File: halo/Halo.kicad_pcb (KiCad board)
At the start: 2 copper layers, 85 x 93 mm, 83 parts, among them J1 USB-C 16P, J2 5V / GND alt, Q1 ALS-PT19-315C, SW1 RESET, SW2 BOOT, SW3 USER, U1 ESP32-C3-MINI-1-N4, U2 AMS1117-3.3, U3 74AHCT1G125

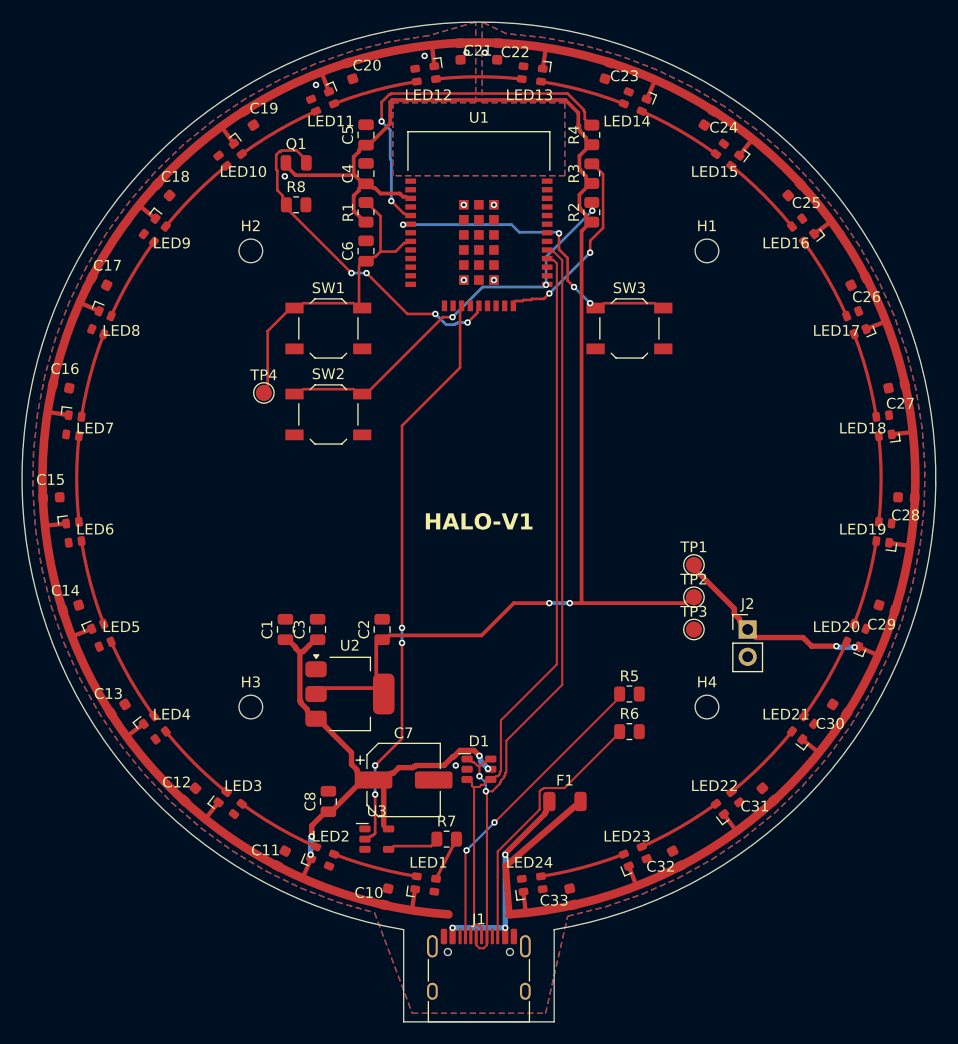
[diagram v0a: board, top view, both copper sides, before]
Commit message: Halo : empreintes ESP32-C3-MINI-1 et WS2812B-2020 d'apres les datasheets, anneau reroute, Gerbers
Verification des empreintes maison contre les datasheets avant les Gerbers :

- ESP32-C3-MINI-1 : l'empreinte "de memoire" placait les 53 broches sur le bord
  du module ; le vrai land pattern (datasheet Espressif v2.2 fig. 11-1, identique
  a espressif/kicad-libraries) a les broches en retrait a x = +/-5.9, rangees
  y = -2.2 / 7.6, masse centrale 3 x 3 (pad 49, un via par pastille), 4 pastilles
  d'angle raccordees par un court segment. Zone antenne 5.4 mm : encoche sans
  cuivre allongee a y = -26.9, keepout de routage ajuste. Table des broches
  (3-1) confirmee identique au schema.
- WS2812B-2020 Worldsemi (LCSC C965555) : brochage reel 1 DO, 2 GND, 3 DI,
  4 VDD, DI et VDD du meme cote. Symbole et empreinte (0.7 x 0.7) refaits ;
  l'anneau tourne desormais dans le sens trigonometrique depuis LED1 en bas a
  droite (impose par le brochage), data DO -> DI en segments droits, 100nF a
  r = 40. Le firmware ne presume rien de la position de LED1.
- SOT-23-5/6 et fusible 1206 aux cotes des bibliotheques KiCad 10 ; trous de
  fixation renommes MountingHole_2.2mm_M2.
- Placement : decouplage et pull-ups le long des vraies broches, F1/C7 et
  U3/R7/C8 permutes gauche/droite pour LED1 a droite. Boutons inchanges (coque).
- Librairies du projet : Halo.kicad_sym, Halo.pretty, sym-lib-table et
  fp-lib-table generes par gen_kicad_libs.py ; ERC a 0.
- Routage du centre refait par route_center.py ; drc.py 0 erreur ; kicad-cli
  pcb drc --refill-zones : 0 non connecte, 0 erreur.
- Gerbers, percage Excellon et fichier de position (kicad-cli 10.0.3) dans
  halo/GERBER_HALO et halo/Halo_GERBER.zip.

Co-Authored-By: Claude Fable 5.1 <noreply@anthropic.com>
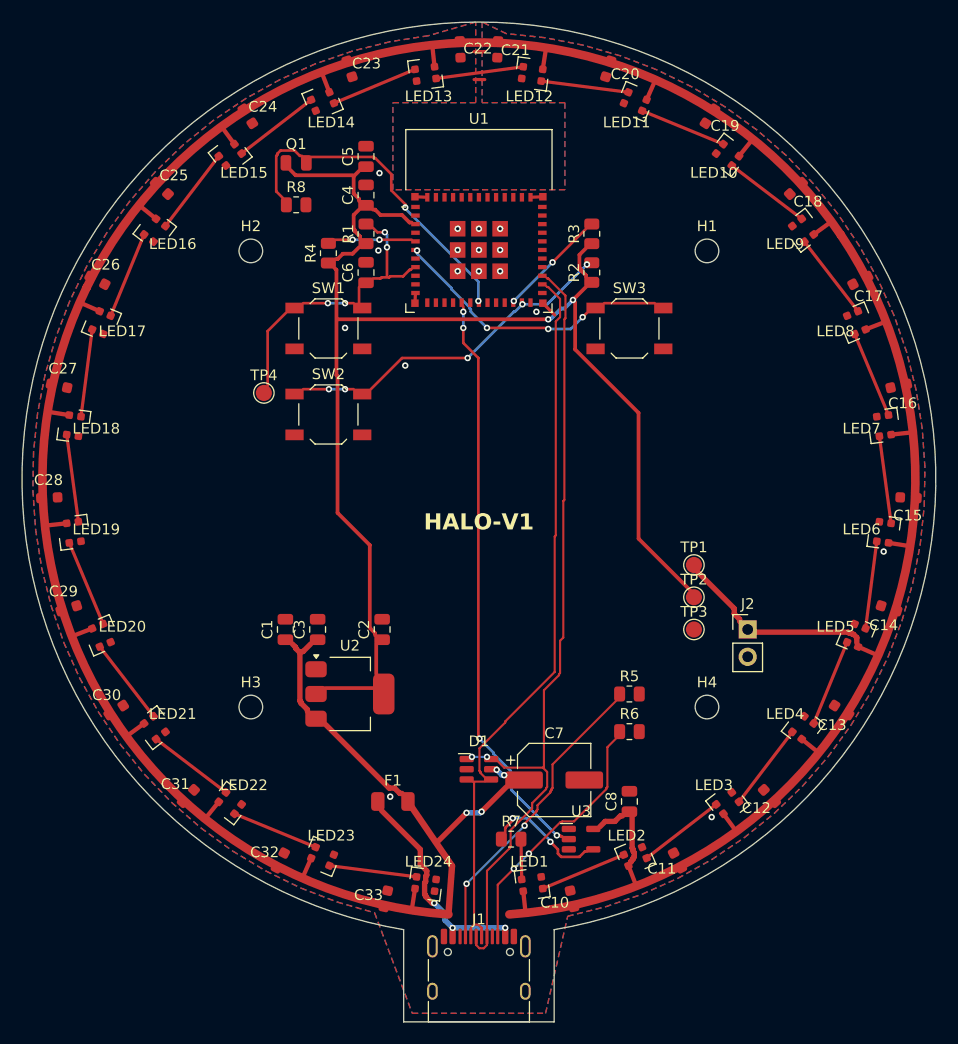
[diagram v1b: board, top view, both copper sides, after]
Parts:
- H1, H2, H3, H4: value MountingHole_2.2mm -> MountingHole_2.2mm_M2; footprint MountingHole:MountingHole_2.2mm -> MountingHole:MountingHole_2.2mm_M2
- U1: footprint RF_Module:ESP32-C3-MINI-1 -> Halo:ESP32-C3-MINI-1
- moved C15 79.7 mm to (190.0, 106.7), turned to 177.5 degrees
- moved C28 79.7 mm to (110.0, 106.7), turned to 2.5 degrees
- moved C16 77.9 mm to (189.1, 96.3), turned to 192.5 degrees
- moved C27 77.9 mm to (110.9, 96.3), turned to 347.5 degrees
- moved C29 76.1 mm to (111.9, 117.0), turned to 17.5 degrees
- moved C14 76.1 mm to (188.1, 117.0), turned to 162.5 degrees
- moved LED18 75.3 mm to (112.3, 100.0), turned to 262.5 degrees
- moved LED19 75.3 mm to (112.3, 110.0), turned to 277.5 degrees
- moved LED6 75.3 mm to (187.7, 110.0), turned to 82.5 degrees
- moved LED7 75.3 mm to (187.7, 100.0), turned to 97.5 degrees
- moved C17 70.8 mm to (185.5, 86.5), turned to 207.5 degrees
- moved C26 70.8 mm to (114.5, 86.5), turned to 332.5 degrees
- moved LED17 70.2 mm to (114.9, 90.5), turned to 247.5 degrees
- moved LED20 70.2 mm to (114.9, 119.5), turned to 292.5 degrees
- moved LED5 70.2 mm to (185.1, 119.5), turned to 67.5 degrees
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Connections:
- LED1 pad 1: 5V -> LED_DIN2
- LED1 pad 2: LED_DIN2 -> GND
- LED1 pad 3: GND -> LED_DIN1
- LED1 pad 4: LED_DIN1 -> 5V
- LED10 pad 1: 5V -> LED_DIN11
- LED10 pad 2: LED_DIN11 -> GND
- LED10 pad 3: GND -> LED_DIN10
- LED10 pad 4: LED_DIN10 -> 5V
- LED11 pad 1: 5V -> LED_DIN12
- LED11 pad 2: LED_DIN12 -> GND
- LED11 pad 3: GND -> LED_DIN11
- LED11 pad 4: LED_DIN11 -> 5V
- LED12 pad 1: 5V -> LED_DIN13
- LED12 pad 2: LED_DIN13 -> GND
- LED12 pad 3: GND -> LED_DIN12
- LED12 pad 4: LED_DIN12 -> 5V
- LED13 pad 1: 5V -> LED_DIN14
- LED13 pad 2: LED_DIN14 -> GND
- LED13 pad 3: GND -> LED_DIN13
- LED13 pad 4: LED_DIN13 -> 5V
- LED14 pad 1: 5V -> LED_DIN15
- LED14 pad 2: LED_DIN15 -> GND
- LED14 pad 3: GND -> LED_DIN14
- LED14 pad 4: LED_DIN14 -> 5V
- LED15 pad 1: 5V -> LED_DIN16
- LED15 pad 2: LED_DIN16 -> GND
- LED15 pad 3: GND -> LED_DIN15
- LED15 pad 4: LED_DIN15 -> 5V
- LED16 pad 1: 5V -> LED_DIN17
- LED16 pad 2: LED_DIN17 -> GND
- LED16 pad 3: GND -> LED_DIN16
- LED16 pad 4: LED_DIN16 -> 5V
- LED17 pad 1: 5V -> LED_DIN18
- LED17 pad 2: LED_DIN18 -> GND
- LED17 pad 3: GND -> LED_DIN17
- LED17 pad 4: LED_DIN17 -> 5V
- LED18 pad 1: 5V -> LED_DIN19
- LED18 pad 2: LED_DIN19 -> GND
- LED18 pad 3: GND -> LED_DIN18
- LED18 pad 4: LED_DIN18 -> 5V
- LED19 pad 1: 5V -> LED_DIN20
- LED19 pad 2: LED_DIN20 -> GND
- LED19 pad 3: GND -> LED_DIN19
- LED19 pad 4: LED_DIN19 -> 5V
- LED2 pad 1: 5V -> LED_DIN3
- LED2 pad 2: LED_DIN3 -> GND
- LED2 pad 3: GND -> LED_DIN2
- LED2 pad 4: LED_DIN2 -> 5V
- LED20 pad 1: 5V -> LED_DIN21
- LED20 pad 2: LED_DIN21 -> GND
- LED20 pad 3: GND -> LED_DIN20
- LED20 pad 4: LED_DIN20 -> 5V
- LED21 pad 1: 5V -> LED_DIN22
- LED21 pad 2: LED_DIN22 -> GND
- LED21 pad 3: GND -> LED_DIN21
- LED21 pad 4: LED_DIN21 -> 5V
- LED22 pad 1: 5V -> LED_DIN23
- LED22 pad 2: LED_DIN23 -> GND
- LED22 pad 3: GND -> LED_DIN22
- LED22 pad 4: LED_DIN22 -> 5V
- LED23 pad 1: 5V -> LED_DIN24
- LED23 pad 2: LED_DIN24 -> GND
- LED23 pad 3: GND -> LED_DIN23
- LED23 pad 4: LED_DIN23 -> 5V
- LED24 pad 1: 5V -> (no net)
- LED24 pad 2: (no net) -> GND
- LED24 pad 3: GND -> LED_DIN24
- LED24 pad 4: LED_DIN24 -> 5V
- LED3 pad 1: 5V -> LED_DIN4
- LED3 pad 2: LED_DIN4 -> GND
- LED3 pad 3: GND -> LED_DIN3
- LED3 pad 4: LED_DIN3 -> 5V
- LED4 pad 1: 5V -> LED_DIN5
- LED4 pad 2: LED_DIN5 -> GND
- LED4 pad 3: GND -> LED_DIN4
- LED4 pad 4: LED_DIN4 -> 5V
- LED5 pad 1: 5V -> LED_DIN6
- LED5 pad 2: LED_DIN6 -> GND
- LED5 pad 3: GND -> LED_DIN5
- LED5 pad 4: LED_DIN5 -> 5V
- LED6 pad 1: 5V -> LED_DIN7
- LED6 pad 2: LED_DIN7 -> GND
- LED6 pad 3: GND -> LED_DIN6
- LED6 pad 4: LED_DIN6 -> 5V
- LED7 pad 1: 5V -> LED_DIN8
- LED7 pad 2: LED_DIN8 -> GND
- LED7 pad 3: GND -> LED_DIN7
- LED7 pad 4: LED_DIN7 -> 5V
- LED8 pad 1: 5V -> LED_DIN9
- LED8 pad 2: LED_DIN9 -> GND
- LED8 pad 3: GND -> LED_DIN8
- LED8 pad 4: LED_DIN8 -> 5V
- LED9 pad 1: 5V -> LED_DIN10
- LED9 pad 2: LED_DIN10 -> GND
- LED9 pad 3: GND -> LED_DIN9
- LED9 pad 4: LED_DIN9 -> 5V
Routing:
- net STRAP_IO2: track 32.3 -> 7.10 mm
- net STRAP_IO8: track 17.4 -> 9.48 mm
- net LED_DATA_5V: track 3.64 -> 10.5 mm, vias 0 -> 2
- net GND: track 0.00 -> 6.81 mm, vias 10 -> 17
- net BOOT: track 33.7 -> 29.3 mm, vias 3 -> 5
- net BTN_USER: track 27.5 -> 24.6 mm
- net 3V3: track 118.7 -> 121.0 mm
- net USB_DM: track 66.7 -> 65.3 mm
- net VBUS: track 17.4 -> 18.7 mm
- net ALS: track 29.4 -> 30.3 mm, vias 4 -> 2
- net LED_DATA_3V3: track 52.5 -> 53.3 mm
- net EN: track 23.7 -> 23.1 mm, vias 0 -> 4
- net CC2: track 23.5 -> 23.0 mm, vias 0 -> 2
- net 5V: track 350.4 -> 349.9 mm, vias 6 -> 4
